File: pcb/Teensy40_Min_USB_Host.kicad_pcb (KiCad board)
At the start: 2 copper layers, 17.8 x 50.8 mm, 17 parts, among them J1 USB_A, J2 Conn_01x14, J3 Conn_01x14, U1 TPD3S014, U2 Teensy4.0

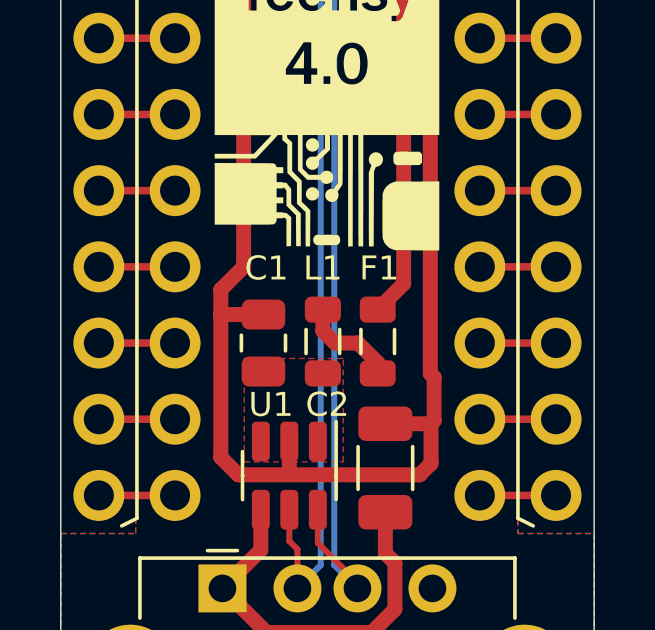
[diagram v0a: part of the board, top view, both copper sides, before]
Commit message: Change fuse footprint
Use the proper 0805 fuse footprint instead of the 0805 inductor footprint.
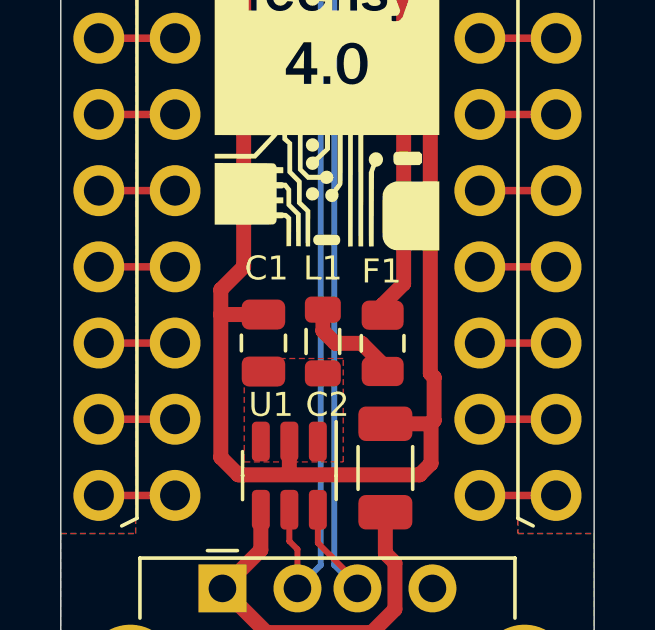
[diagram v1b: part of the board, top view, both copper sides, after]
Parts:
- F1: footprint Inductor_SMD:L_0805_2012Metric -> Fuse:Fuse_0805_2012Metric
- moved F1 0.17 mm to (151.7, 110.5)
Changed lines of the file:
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@@
     )
   )
-  (footprint "Inductor_SMD:L_0805_2012Metric" (layer "F.Cu")
-    (at 151.5364 110.4392 -90)
-    (descr "Inductor SMD 0805 (2012 Metric), square (rectangular) end terminal, IPC_7351 nominal, (Body size source: IPC-SM-782 page 80, https://www.pcb-3d.com/wordpress/wp-content/uploads/ipc-sm-782a_amendment_1_and_2.pdf), generated with kicad-footprint-generator")
-    (tags "inductor")
+  (footprint "Fuse:Fuse_0805_2012Metric" (layer "F.Cu")
+    (at 151.7 110.5 -90)
+    (descr "Fuse SMD 0805 (2012 Metric), square (rectangular) end terminal, IPC_7351 nominal, (Body size source: https://docs.google.com/spreadsheets/d/1BsfQQcO9C6DZCsRaXUlFlo91Tg2WpOkGARC1WS5S8t0/edit?usp=sharing), generated with kicad-footprint-generator")
+    (tags "fuse")
     (property "Description" "PTC RESET FUSE 6V 500MA 0805")
     (property "DigiKey Product Number" "283-PTS08056V050CT-ND")
@@
     (property "Sheetname" "")
     (attr smd)
-    (fp_text reference "F1" (at -2.4392 -0.05) (layer "F.SilkS")
+    (fp_text reference "F1" (at -2.4 0.0364) (layer "F.SilkS")
       (effects (font (size 0.8 0.8) (thickness 0.15)))
     )
-    (fp_text value "500 mA" (at -4.7752 0.0254 90) (layer "F.Fab")
+    (fp_text value "500 mA" (at 0 -2.9636) (layer "F.Fab") hide
       (effects (font (size 1 1) (thickness 0.15)))
     )
-    (fp_text user "${REFERENCE}" (at 0 0 90) (layer "F.Fab")
+    (fp_text user "${REFERENCE}" (at 0 0 -90) (layer "F.Fab")
       (effects (font (size 0.5 0.5) (thickness 0.08)))
     )
-    (fp_line (start -0.399622 0.56) (end 0.399622 0.56) (layer "F.SilkS") (width 0.12))
-    (fp_line (start -0.399622 -0.56) (end 0.399622 -0.56) (layer "F.SilkS") (width 0.12))
-    (fp_line (start -1.75 -0.85) (end 1.75 -0.85) (layer "F.CrtYd") (width 0.05))
-    (fp_line (start 1.75 0.85) (end -1.75 0.85) (layer "F.CrtYd") (width 0.05))
-    (fp_line (start 1.75 -0.85) (end 1.75 0.85) (layer "F.CrtYd") (width 0.05))
-    (fp_line (start -1.75 0.85) (end -1.75 -0.85) (layer "F.CrtYd") (width 0.05))
-    (fp_line (start 1 -0.45) (end 1 0.45) (layer "F.Fab") (width 0.1))
-    (fp_line (start 1 0.45) (end -1 0.45) (layer "F.Fab") (width 0.1))
-    (fp_line (start -1 -0.45) (end 1 -0.45) (layer "F.Fab") (width 0.1))
-    (fp_line (start -1 0.45) (end -1 -0.45) (layer "F.Fab") (width 0.1))
-    (pad "1" smd roundrect locked (at -1.0625 0 270) (size 0.875 1.2) (layers "F.Cu" "F.Paste" "F.Mask") (roundrect_rratio 0.25)
+    (fp_line (start -0.258578 0.71) (end 0.258578 0.71) (layer "F.SilkS") (width 0.12))
+    (fp_line (start -0.258578 -0.71) (end 0.258578 -0.71) (layer "F.SilkS") (width 0.12))
+    (fp_line (start -1.68 0.95) (end -1.68 -0.95) (layer "F.CrtYd") (width 0.05))
+    (fp_line (start 1.68 -0.95) (end 1.68 0.95) (layer "F.CrtYd") (width 0.05))
+    (fp_line (start 1.68 0.95) (end -1.68 0.95) (layer "F.CrtYd") (width 0.05))
+    (fp_line (start -1.68 -0.95) (end 1.68 -0.95) (layer "F.CrtYd") (width 0.05))
+    (fp_line (start -1 0.6) (end -1 -0.6) (layer "F.Fab") (width 0.1))
+    (fp_line (start 1 0.6) (end -1 0.6) (layer "F.Fab") (width 0.1))
+    (fp_line (start -1 -0.6) (end 1 -0.6) (layer "F.Fab") (width 0.1))
+    (fp_line (start 1 -0.6) (end 1 0.6) (layer "F.Fab") (width 0.1))
+    (pad "1" smd roundrect (at -0.9375 0 270) (size 0.975 1.4) (layers "F.Cu" "F.Paste" "F.Mask") (roundrect_rratio 0.25)
       (net 1 "VCC") (pintype "passive"))
-    (pad "2" smd roundrect locked (at 1.0625 0 270) (size 0.875 1.2) (layers "F.Cu" "F.Paste" "F.Mask") (roundrect_rratio 0.25)
+    (pad "2" smd roundrect (at 0.9375 0 270) (size 0.975 1.4) (layers "F.Cu" "F.Paste" "F.Mask") (roundrect_rratio 0.25)
       (net 6 "Net-(F1-Pad2)") (pintype "passive"))
-    (model "${KICAD6_3DMODEL_DIR}/Inductor_SMD.3dshapes/L_0805_2012Metric.wrl"
+    (model "${KICAD6_3DMODEL_DIR}/Fuse.3dshapes/Fuse_0805_2012Metric.wrl"
       (offset (xyz 0 0 0))
       (scale (xyz 1 1 1))
@@
   (segment (start 157.48 82.55) (end 154.94 82.55) (width 0.5) (layer "F.Cu") (net 1))
   (segment (start 153.416 84.074) (end 154.94 82.55) (width 0.5) (layer "F.Cu") (net 1))
-  (segment (start 151.5364 109.3767) (end 152.4 108.5131) (width 0.5) (layer "F.Cu") (net 1))
+  (segment (start 151.7 109.5625) (end 151.7 109.2131) (width 0.5) (layer "F.Cu") (net 1))
   (segment (start 153.416 85.293865) (end 153.416 84.074) (width 0.5) (layer "F.Cu") (net 1))
   (segment (start 152.4 108.5131) (end 152.4 86.309865) (width 0.5) (layer "F.Cu") (net 1))
   (segment (start 152.4 86.309865) (end 153.416 85.293865) (width 0.5) (layer "F.Cu") (net 1))
+  (segment (start 151.7 109.2131) (end 152.4 108.5131) (width 0.5) (layer "F.Cu") (net 1))
   (segment (start 147.066 107.95) (end 147.066 85.09) (width 0.5) (layer "F.Cu") (net 2))
   (segment (start 146.88812 114.88412) (end 152.93348 114.88412) (width 0.5) (layer "F.Cu") (net 2))
@@
   (segment (start 147.71952 91.817015) (end 147.71952 88.455317) (width 0.2) (layer "B.Cu") (net 5))
   (segment (start 150.085001 94.182496) (end 147.71952 91.817015) (width 0.2) (layer "B.Cu") (net 5))
-  (segment (start 151.5364 111.5017) (end 151.5364 111.1504) (width 0.5) (layer "F.Cu") (net 6))
   (segment (start 149.7076 109.3767) (end 149.7076 110.0836) (width 0.5) (layer "F.Cu") (net 6))
-  (segment (start 149.7076 110.0836) (end 150.114 110.49) (width 0.5) (layer "F.Cu") (net 6))
-  (segment (start 150.876 110.49) (end 150.114 110.49) (width 0.5) (layer "F.Cu") (net 6))
-  (segment (start 151.5364 111.1504) (end 150.876 110.49) (width 0.5) (layer "F.Cu") (net 6))
+  (segment (start 151 110.5) (end 151.7 111.2) (width 0.5) (layer "F.Cu") (net 6))
+  (segment (start 150.124 110.5) (end 151 110.5) (width 0.5) (layer "F.Cu") (net 6))
+  (segment (start 151.7 111.2) (end 151.7 111.4375) (width 0.5) (layer "F.Cu") (net 6))
+  (segment (start 149.7076 110.0836) (end 150.124 110.5) (width 0.5) (layer "F.Cu") (net 6))
   (segment (start 142.24 115.57) (end 144.78 115.57) (width 0.25) (layer "F.Cu") (net 7))
   (segment (start 144.78 113.03) (end 142.24 113.03) (width 0.25) (layer "F.Cu") (net 8))

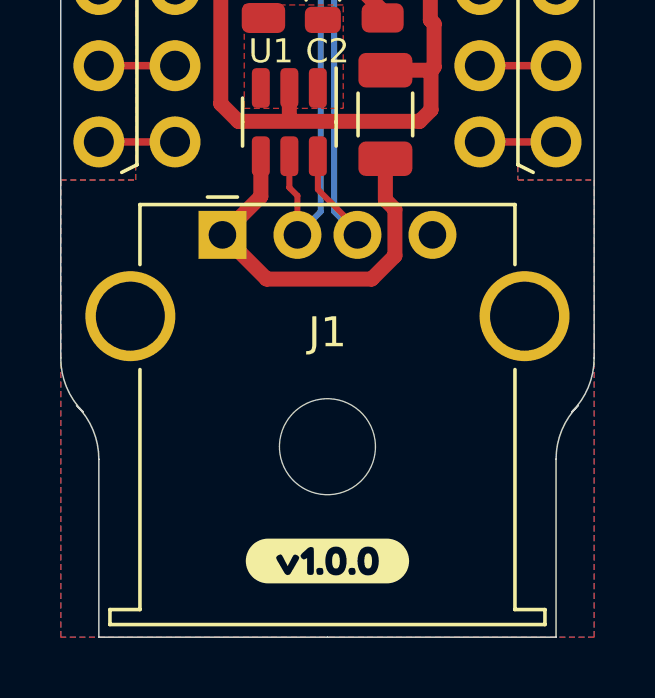
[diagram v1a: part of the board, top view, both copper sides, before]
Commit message: Move board edge back by 0.2"
Allows space for the USB-A port to integrate into a panel or case.

With the smaller size, the alignment hole at the USB-A port has been moved to make a half-circle cut at the board edge. This changes the distance between alignment holes from 1.4" to 1.45".
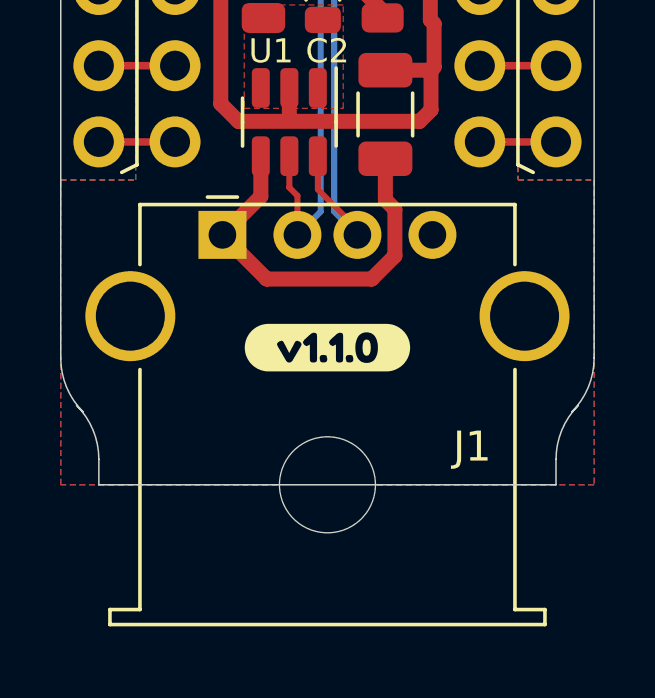
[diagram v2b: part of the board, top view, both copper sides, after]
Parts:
- removed kibuzzard-61E33C7E: G***, kibuzzard-61E33C7E
- removed kibuzzard-61E44D65: G***, kibuzzard-61E44D65
- added kibuzzard-621DE22F: G***, kibuzzard-621DE22F, F.Cu at (149.9, 122.4)
- added kibuzzard-621DE35D: G***, kibuzzard-621DE35D, B.Cu at (149.9, 121.2)
- added kibuzzard-621DE366: G***, kibuzzard-621DE366, B.Cu at (149.9, 123.7)
- moved H2 1.27 mm to (149.9, 127.0)
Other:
- board size 17.8 x 50.8 mm -> 17.8 x 45.7 mm

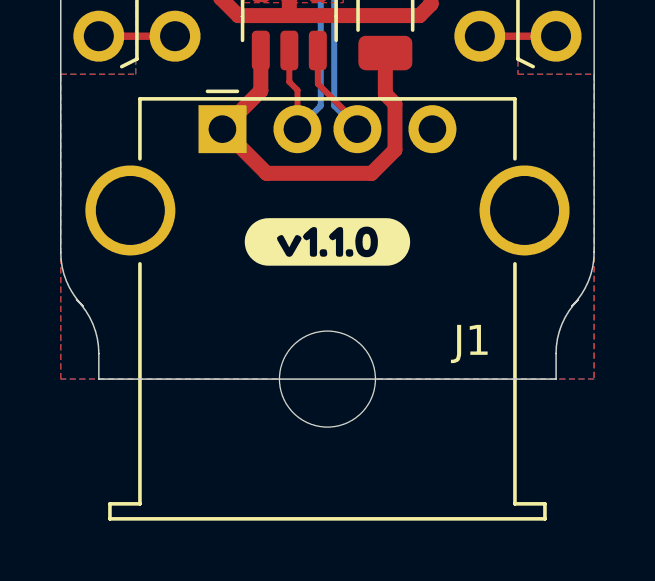
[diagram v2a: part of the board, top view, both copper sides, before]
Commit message: Move alignment hole back to original position
This makes the alignment hole position and distance (1.4") the same between v1.0.0 and v1.1.0. For what that's worth.
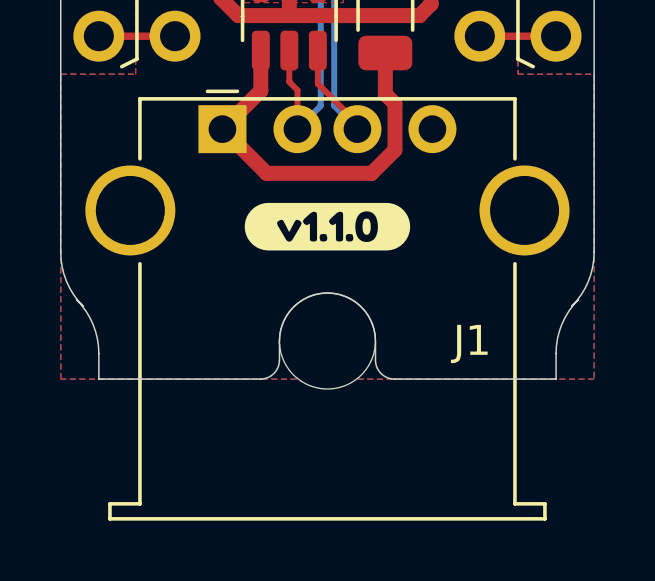
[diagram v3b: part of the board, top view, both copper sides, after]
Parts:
- removed kibuzzard-621DE35D: G***, kibuzzard-621DE35D
- removed kibuzzard-621DE366: G***, kibuzzard-621DE366
- added kibuzzard-621DEA3B: G***, kibuzzard-621DEA3B, B.Cu at (149.9, 121.9)
- moved H2 1.27 mm to (149.9, 125.7)
- moved kibuzzard-621DE22F 0.51 mm to (149.9, 121.9)
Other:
- outline, holes or cut-outs redrawn
